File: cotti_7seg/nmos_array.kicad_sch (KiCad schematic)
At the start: 8 parts, among them Q1 NMOS Vth=0,7 Kp=1,5, Q2 NMOS Vth=0,7 Kp=1,5, Q3 NMOS Vth=0,7 Kp=1,5, Q4 NMOS Vth=0,7 Kp=1,5, Q5 NMOS Vth=0,7 Kp=1,5, Q6 NMOS Vth=0,7 Kp=1,5, Q7 NMOS Vth=0,7 Kp=1,5, Q8 NMOS Vth=0,7 Kp=1,5

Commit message: feat: cotti 7seg gerbers
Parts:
- removed Q1, Q2, Q3, Q4, Q5, Q6, Q7, Q8: NMOS Vth=0,7 Kp=1,5, project_footprints:DIO_RB558WMF_ROM-L, symbol Simulation_SPICE:NMOS
- added Q1, Q2, Q3, Q4, Q5, Q6, Q7, Q8: RE1C001UNTCL, cotti_footprints:SOT-416, symbol cotti_transistors:RE1C001UNTCL
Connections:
- net VCC: now also Q1.3 (D), Q2.3 (D), Q3.3 (D), Q4.3 (D), Q5.3 (D), Q6.3 (D), Q7.3 (D), Q8.3 (D)
- net a_in: now also Q1.1 (G)
- net a_out: now also Q1.2 (S)
- net b_in: now also Q2.1 (G)
- net b_out: now also Q2.2 (S)
- net c_in: now also Q3.1 (G)
- net c_out: now also Q3.2 (S)
- net d_in: now also Q4.1 (G)
- net d_out: now also Q4.2 (S)
- net dp_in: now also Q7.1 (G)
- net dp_out: now also Q7.2 (S)
- net e_in: now also Q8.1 (G)
- net e_out: now also Q8.2 (S)
- net f_in: now also Q5.1 (G)
- net f_out: now also Q5.2 (S)
- net g_in: now also Q6.1 (G)
- net g_out: now also Q6.2 (S)
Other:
- company: (none) -> Cotti
- title: (none) -> 7Seg Module

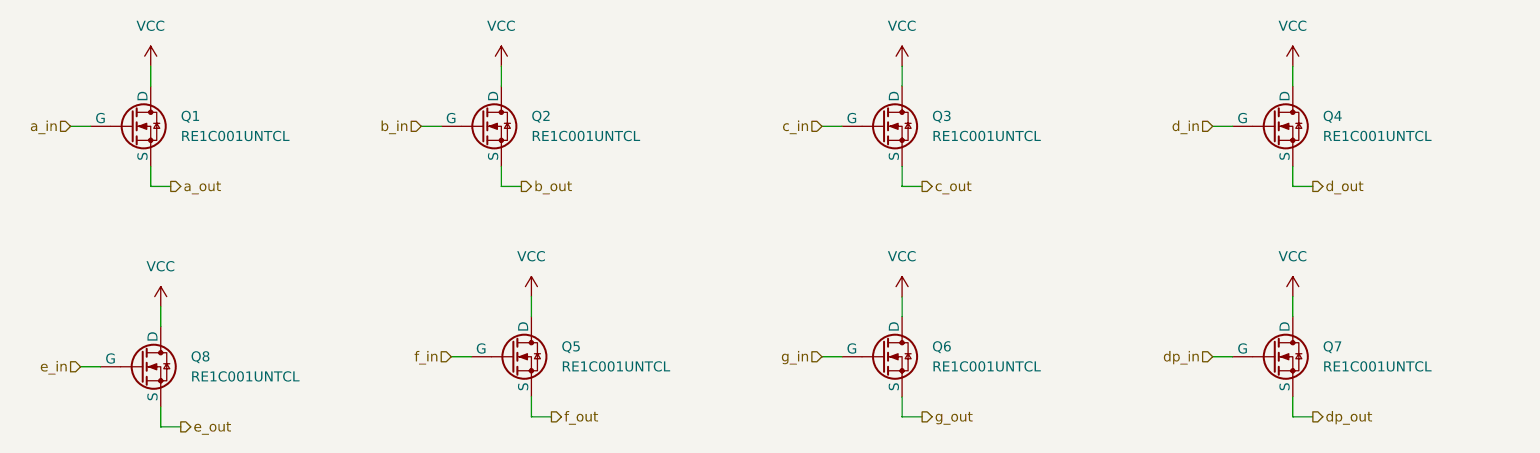
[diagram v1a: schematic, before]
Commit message: fix: change "vcc" to "3v3" power input
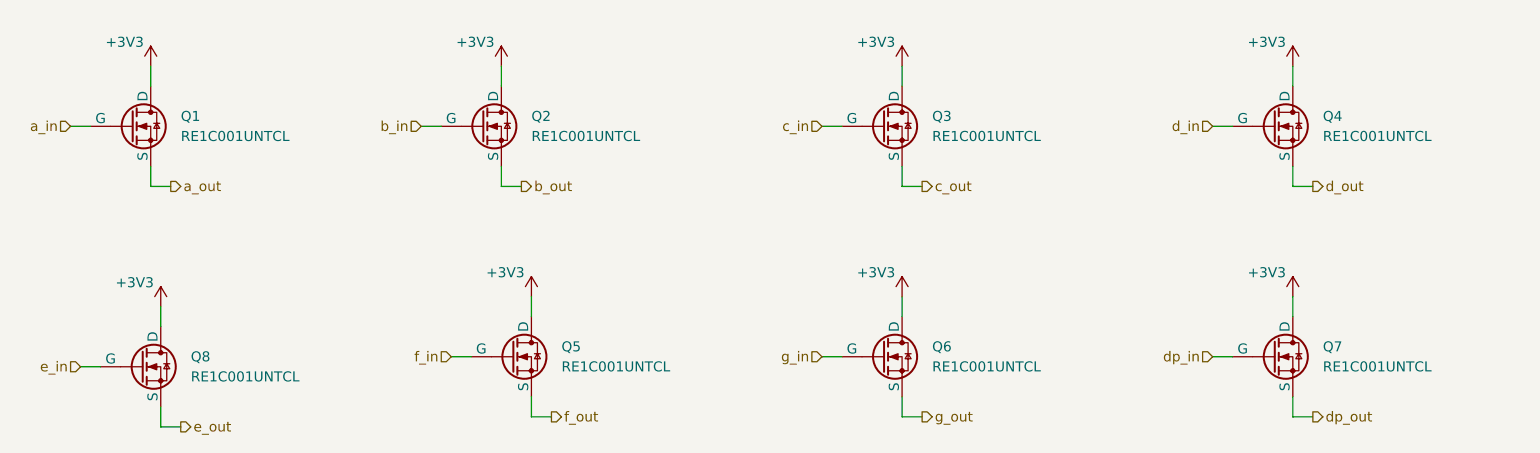
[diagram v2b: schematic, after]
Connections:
- net VCC renamed +3V3
